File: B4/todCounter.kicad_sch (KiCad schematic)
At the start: 0 parts

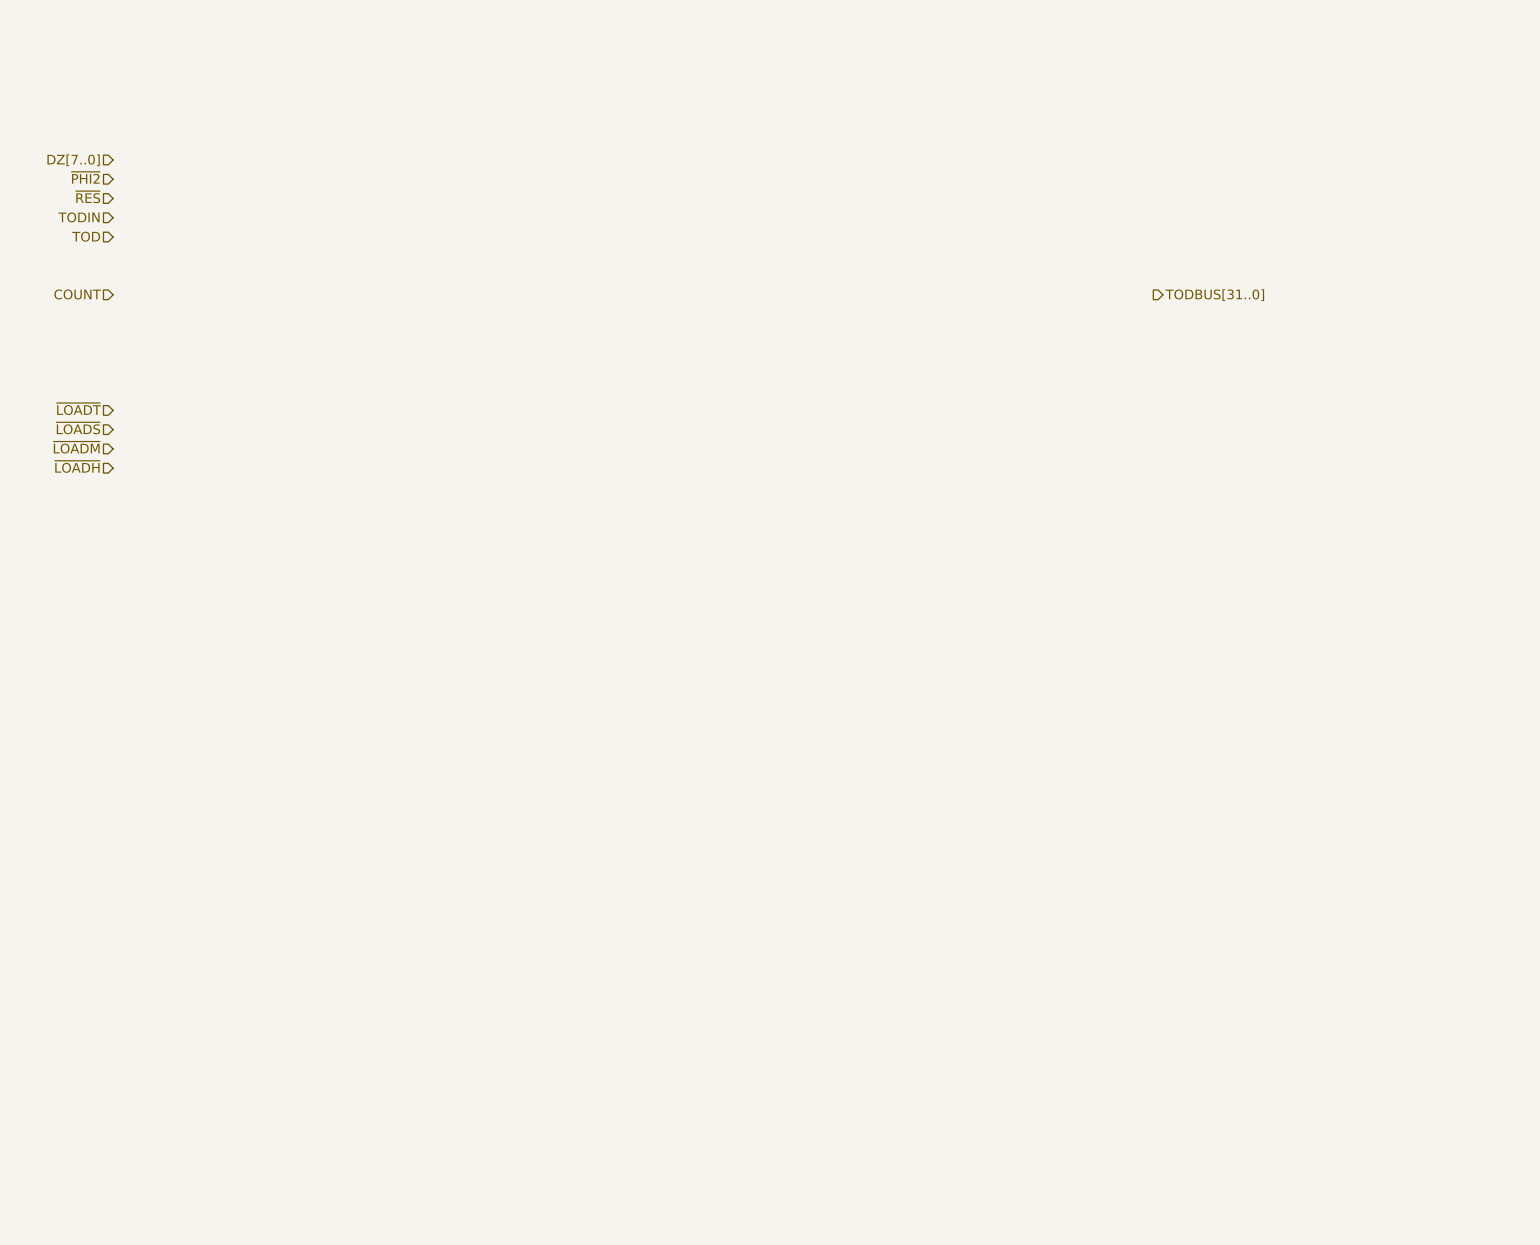
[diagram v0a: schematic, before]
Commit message: B2 refactored. B4 Added. TOD sch completed.
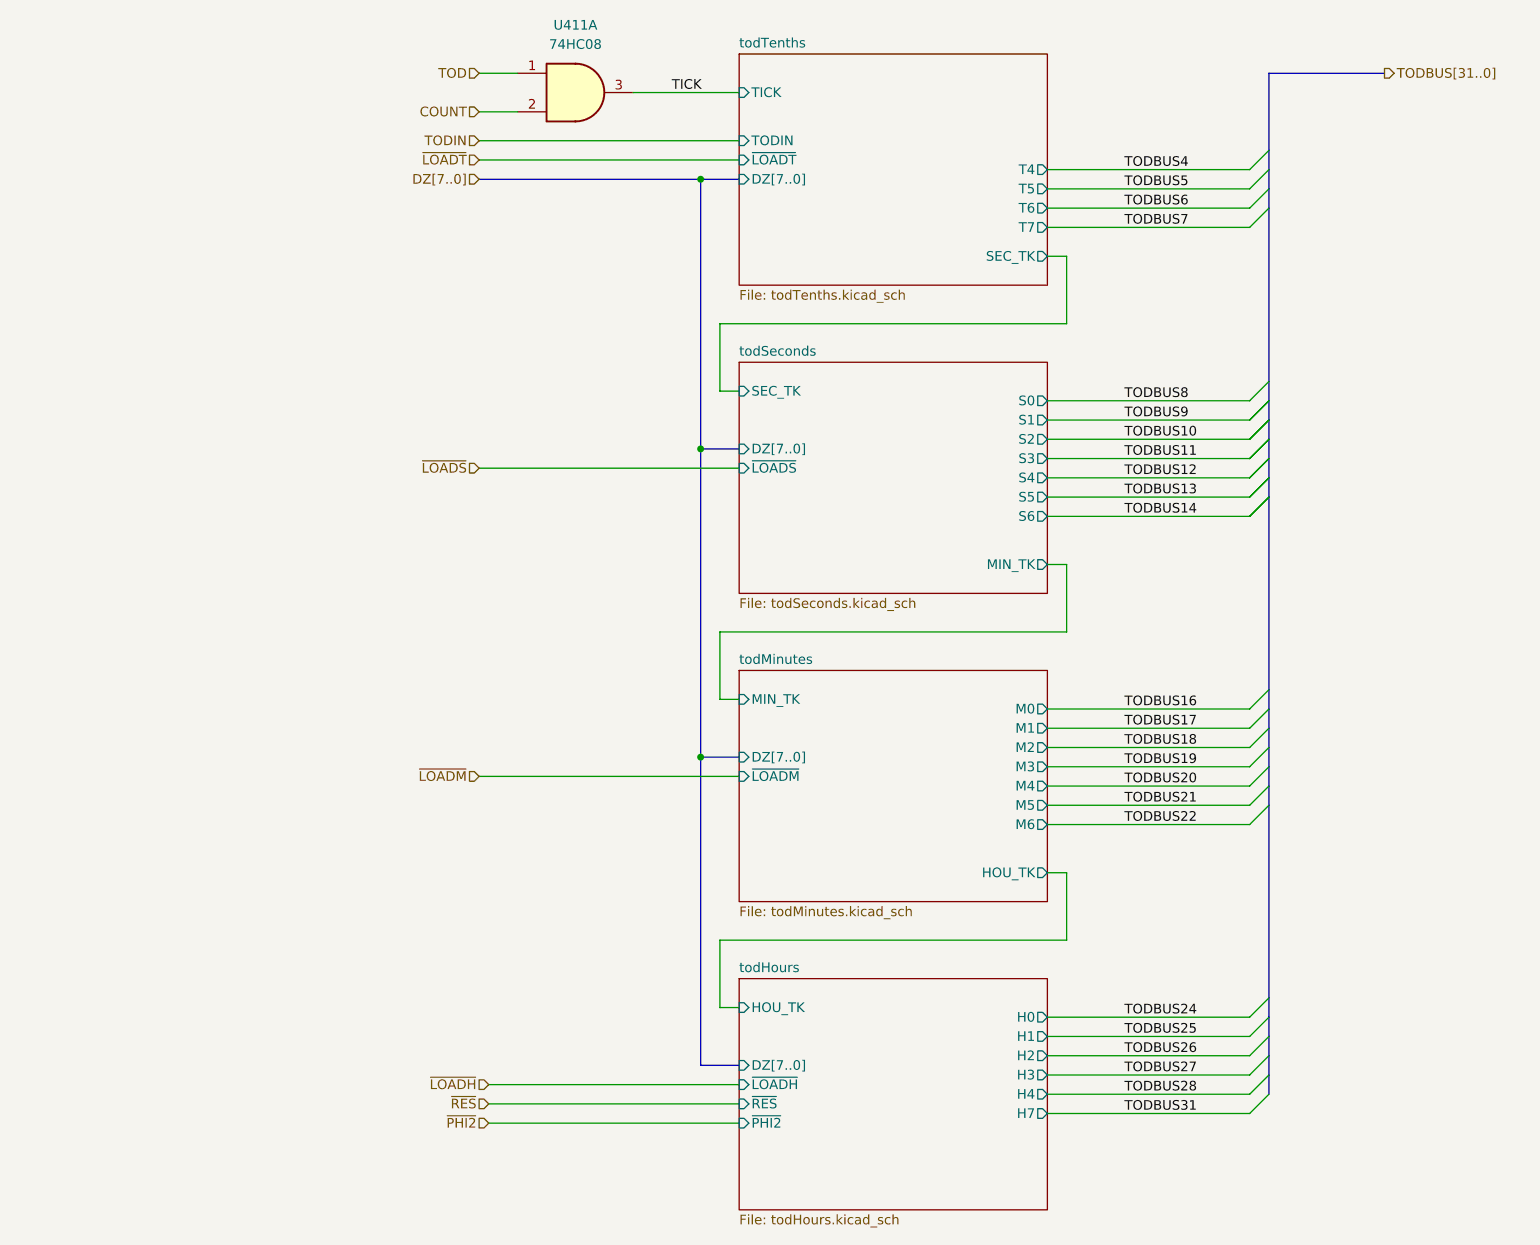
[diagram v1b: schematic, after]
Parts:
- added U411: 74HC08, Package_SO:SOIC-14_3.9x8.7mm_P1.27mm, symbol Custom 74xx:74HC08
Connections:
- net COUNT: now also U411.2
- net TOD: now also U411.1
- new net TICK: U411.3
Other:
- added sheet todHours (todHours.kicad_sch)
- added sheet todMinutes (todMinutes.kicad_sch)
- added sheet todSeconds (todSeconds.kicad_sch)
- added sheet todTenths (todTenths.kicad_sch)

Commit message: TOD is here
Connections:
- net COUNT: now also U411.10; no longer U411.2
- net TICK: now also U411.8; no longer U411.3
- net TOD: now also U411.9; no longer U411.1
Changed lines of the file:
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@@
     (effects (font (size 1.27 1.27)) (justify right))
   )
-  (symbol (lib_id "Custom 74xx:74HC08") (at 109.22 26.67 0) (unit 1)
+  (symbol (lib_id "Custom 74xx:74HC08") (at 109.22 26.67 0) (unit 3)
     (in_bom yes) (on_board yes) (fields_autoplaced)
     (property "Reference" "U411" (id 0) (at 109.22 17.78 0))

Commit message: .
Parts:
- U411: value 74HC08 -> 74HCT08
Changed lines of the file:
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@@
     (in_bom yes) (on_board yes) (fields_autoplaced)
     (property "Reference" "U411" (id 0) (at 109.22 17.78 0))
-    (property "Value" "74HC08" (id 1) (at 109.22 20.32 0))
+    (property "Value" "74HCT08" (id 1) (at 109.22 20.32 0))
     (property "Footprint" "Package_SO:SOIC-14_3.9x8.7mm_P1.27mm" (id 2) (at 109.22 26.67 0)
       (effects (font (size 1.27 1.27)) hide)

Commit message: Ready for v0.2.2
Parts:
- renumbered U411 to U435
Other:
- company: (none) -> Daniel Molina
- title: (none) -> 74HCT6526 Board 4
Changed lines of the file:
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@@
 (kicad_sch (version 20211123) (generator eeschema)
   (paper "A4")
+  (title_block
+    (title "74HCT6526 Board 4")
+    (date "2023-06-22")
+    (rev "0.2.2")
+    (company "Daniel Molina")
+    (comment 1 "https://github.com/dmolinagarcia/74HCT6526")
+  )
   (junction (at 125.73 73.66) (diameter 0) (color 0 0 0 0)
   )
@@
   (symbol (lib_id "Custom 74xx:74HC08") (at 109.22 26.67 0) (unit 3)
     (in_bom yes) (on_board yes) (fields_autoplaced)
-    (property "Reference" "U411" (id 0) (at 109.22 17.78 0))
+    (property "Reference" "U435" (id 0) (at 109.22 17.78 0))
     (property "Value" "74HCT08" (id 1) (at 109.22 20.32 0))
     (property "Footprint" "Package_SO:SOIC-14_3.9x8.7mm_P1.27mm" (id 2) (at 109.22 26.67 0)
